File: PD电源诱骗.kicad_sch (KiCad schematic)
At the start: 33 parts, among them J1 USB_C_Receptacle_USB2.0_16P, J2 电源IO, U1 TPS5430DDA, U2 CH224A, U3 XL6019

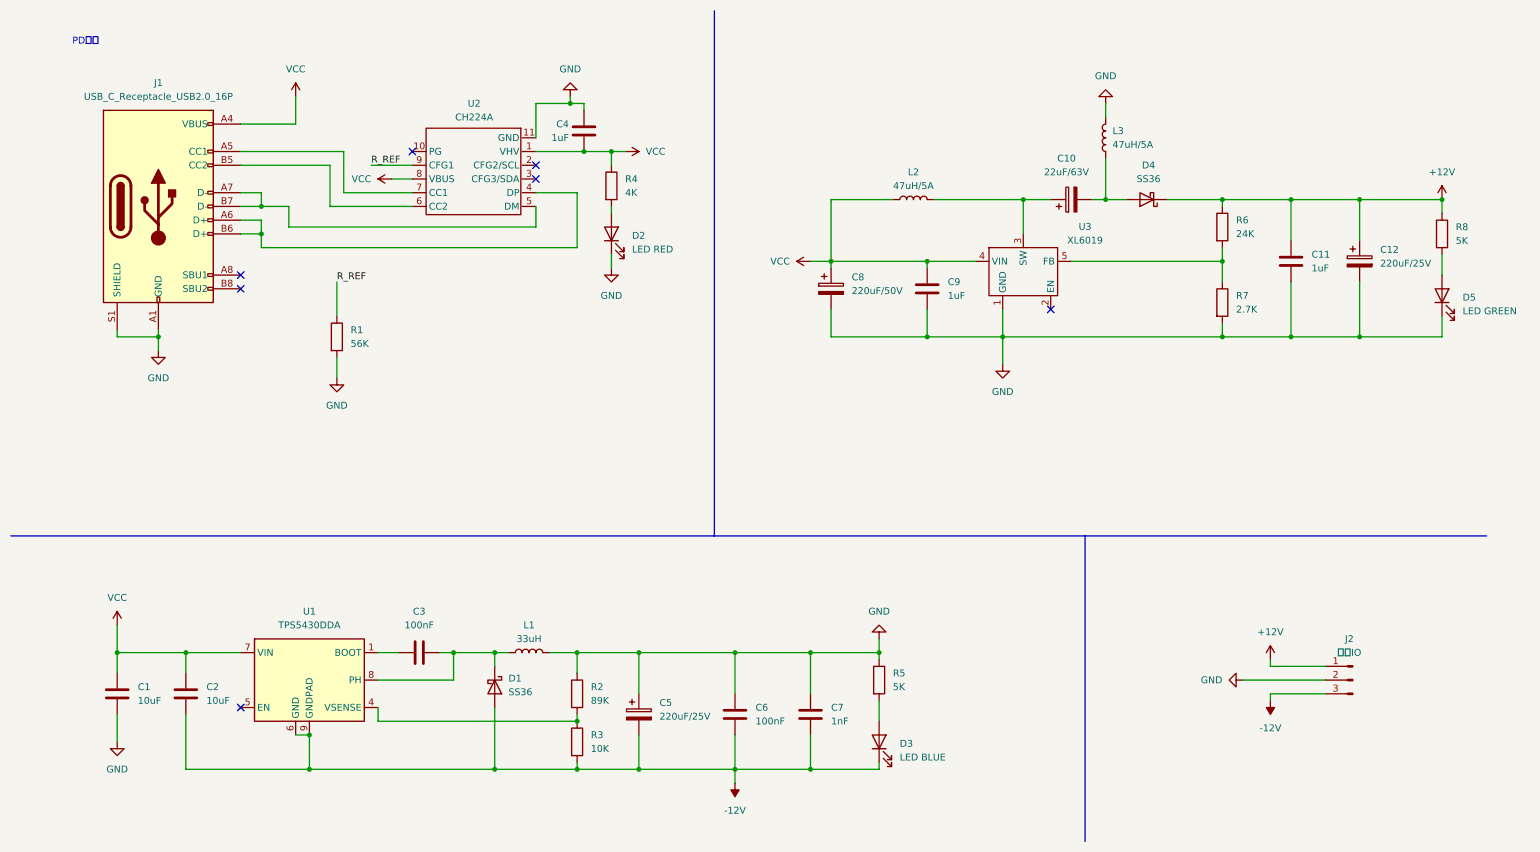
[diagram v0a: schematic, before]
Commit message: 修改为诱骗9V+BOOST得到12V
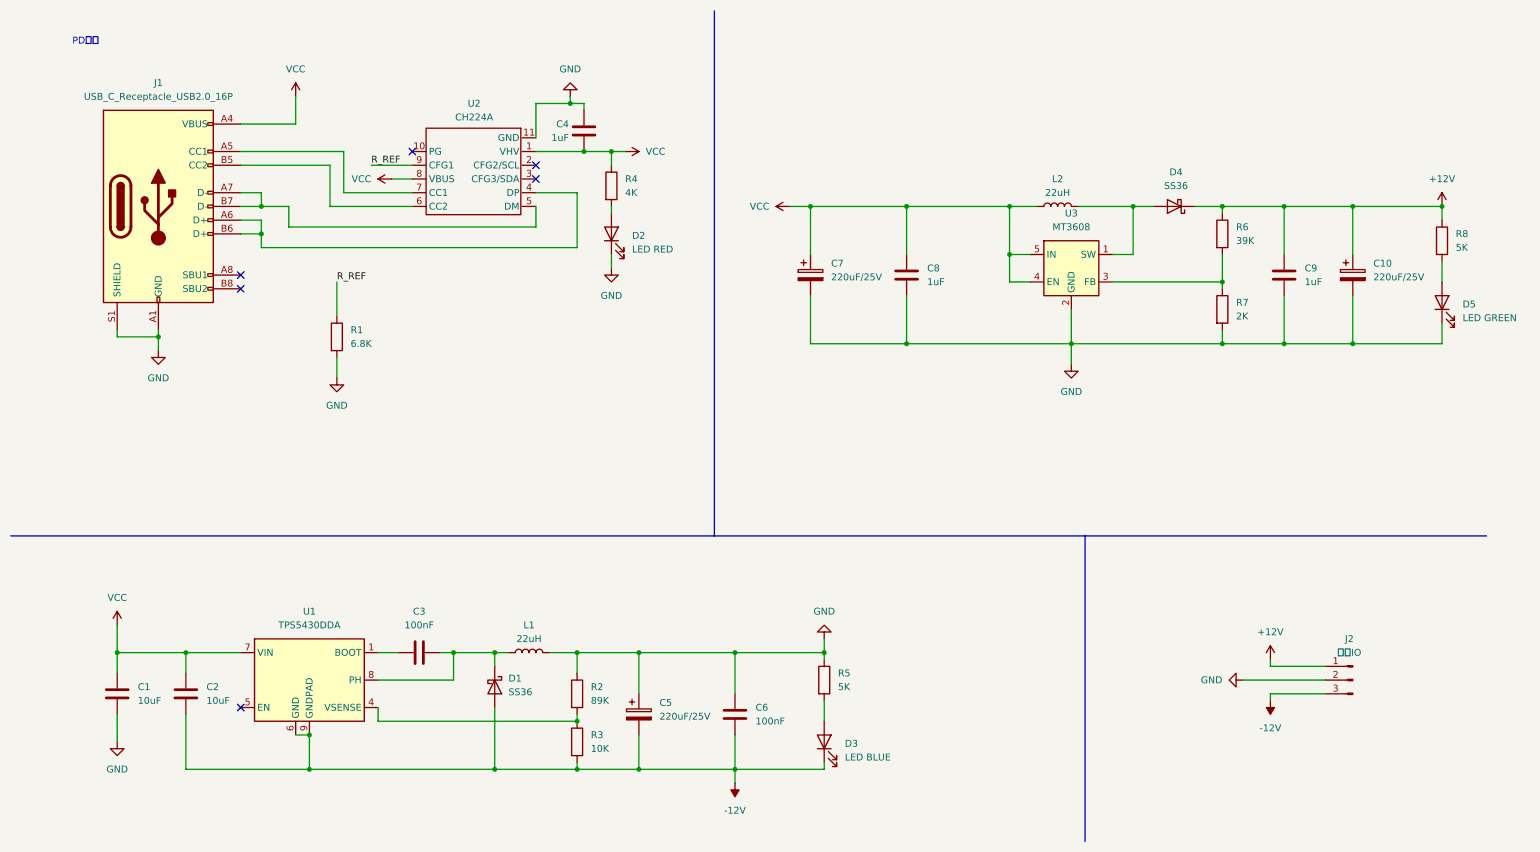
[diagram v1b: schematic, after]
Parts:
- removed C10: 22uF/63V, Capacitor_SMD:CP_Elec_6.3x7.7, symbol Device:C_Polarized
- removed C7: 1nF, Capacitor_SMD:C_0805_2012Metric, symbol Device:C
- removed C8: 220uF/50V, Capacitor_SMD:CP_Elec_10x10.5, symbol Device:C_Polarized
- removed C9: 1uF, Capacitor_SMD:C_0805_2012Metric, symbol Device:C
- removed L3: 47uH/5A, Inductor_SMD:L_Wuerth_HCI-1040, symbol Device:L
- removed U3: XL6019, Package_TO_SOT_SMD:TO-263-5_TabPin3, symbol MyLib:XL6019
- added C7: 220uF/25V, Capacitor_SMD:CP_Elec_8x10.5, symbol Device:C_Polarized
- added C8: 1uF, Capacitor_SMD:C_0805_2012Metric, symbol Device:C
- added U3: MT3608, Package_TO_SOT_SMD:SOT-23-6, symbol Regulator_Switching:MT3608
- L1: value 33uH -> 22uH
- L2: value 47uH/5A -> 22uH; footprint Inductor_SMD:L_Wuerth_HCI-1040 -> Inductor_SMD:L_TechFuse_SL0630
- R1: value 56K -> 6.8K
- R6: value 24K -> 39K
- R7: value 2.7K -> 2K
- renumbered C12 to C10, C11 to C9
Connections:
- net GND: now also C7.2, C8.2, U3.2 (GND)
- net VCC: now also C7.1, C8.1, U3.4 (EN), U3.5 (IN)
- net at R6.2, R7.1: now also U3.3 (FB)
- net at L2.2: now also D4.2 (A), U3.1 (SW)
- no-connect marks 7 -> 6
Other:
- moved on the sheet: C10, C9, D3, D5, R5, R6, R7, R8
